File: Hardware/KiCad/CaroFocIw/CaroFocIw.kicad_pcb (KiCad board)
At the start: 4 copper layers, 174.5 x 99 mm, 110 parts, among them J1 Conn_01x04, J10 Conn_01x03, J11 Conn_01x06, J12 Conn_01x06, J13 Conn_01x02, J14 Conn_01x03, J15 Conn_01x03, J16 Conn_01x03, J17 Conn_01x02, J18 Conn_01x03, J19 Conn_01x03, J2 Conn_01x02, J20 Conn_01x03, J21 Conn_01x06, J22 Conn_01x06, J23 Conn_01x02, J24 Conn_01x03, J25 Conn_01x03, J26 Conn_01x03, J3 Conn_01x01, J4 Conn_01x01, J5 Conn_01x01, J6 Conn_01x01, J7 Conn_01x02, J8 Conn_01x03, J9 Conn_01x03, Q1 Q_NMOS_SGD, Q2 Q_NMOS_SGD, Q3 Q_NMOS_SGD, Q4 Q_NMOS_SGD, Q5 Q_NMOS_SGD, Q6 Q_NMOS_SGD, U1 TCAN332, U2 STM32F405RGTx, U3 TLE7185-1E, U4 ACS711xEXLT-15AB, U5 AS5048A, U6 ACS711xEXLT-15AB, U7 ACS711xEXLT-15AB, U8 LMR16006YQ3

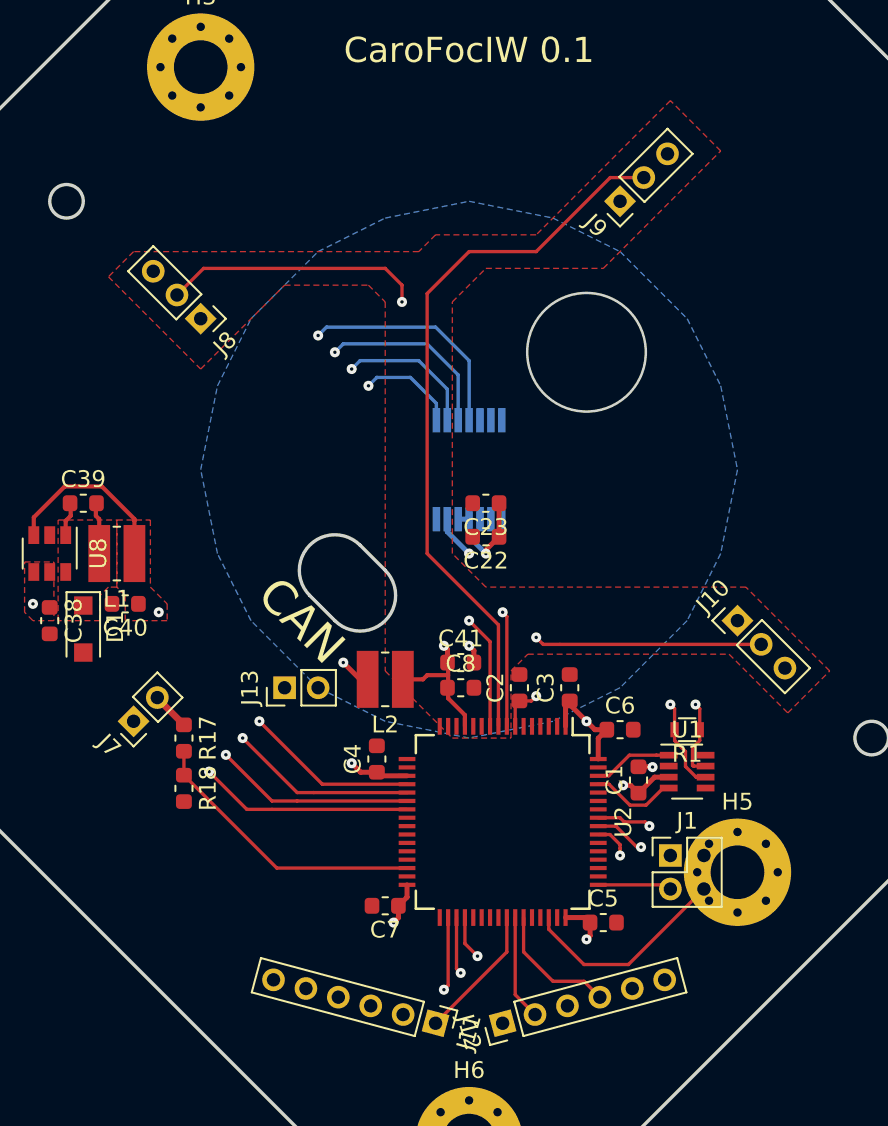
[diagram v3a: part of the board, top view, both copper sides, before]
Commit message: Changed footprint of one inductor, rerouted microcontroller part. Mounting hole placement still needs some thoughts...
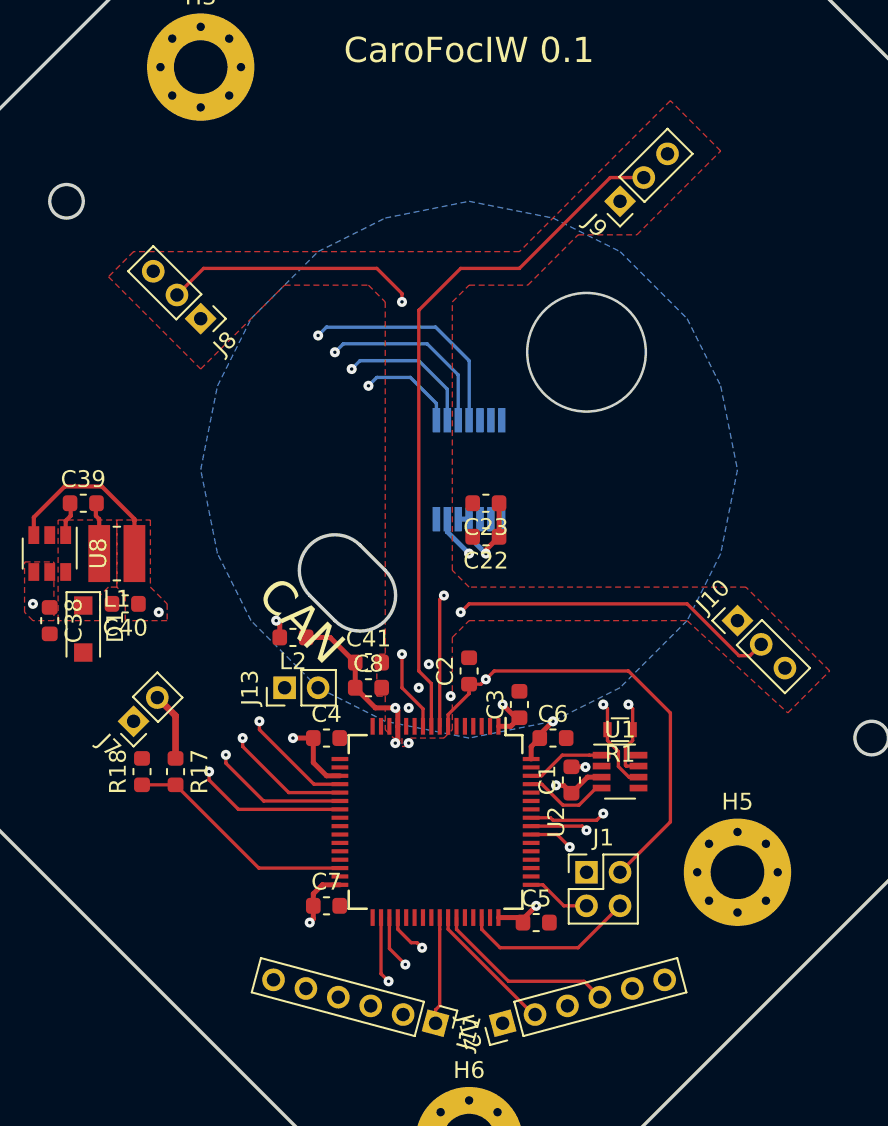
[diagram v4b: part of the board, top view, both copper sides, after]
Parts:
- L2: footprint Inductors_SMD:L_Wuerth_MAPI-3015 -> Inductor_SMD:L_0603_1608Metric
- moved L2 6.04 mm to (109.5, 135.0)
- moved C41 5.50 mm to (114.0, 136.5)
- moved C8 5.50 mm to (114.0, 138.0)
- moved J1 5.10 mm to (127.0, 149.0)
- moved C6 4.03 mm to (125.0, 141.0)
- moved C1 4.00 mm to (126.1, 143.5)
- moved C5 4.00 mm to (124.0, 152.0)
- moved R1 4.00 mm to (129.0, 140.5)
- moved U1 4.00 mm to (129.0, 143.0)
- moved U2 4.00 mm to (118.0, 146.0)
- moved C7 3.50 mm to (111.5, 151.0), turned to 0 degrees
- moved C4 3.25 mm to (111.5, 141.0), turned to 0 degrees
- moved C2 3.16 mm to (120.0, 137.0)
- moved C3 3.16 mm to (123.0, 139.0)
- moved R18 2.69 mm to (100.5, 143.0), turned to 90 degrees
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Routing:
- net /MCU/CurrentW: track 24.8 -> 29.0 mm
- net /Encoder/EncoderMiso: track 50.1 -> 46.4 mm
- net /Encoder/~EncoderCs: track 39.4 -> 35.7 mm
- net /Encoder/EncoderMosi: track 55.4 -> 51.7 mm
- net /Encoder/EncoderSclk: track 44.7 -> 41.0 mm
- net /Can/CanL: track 29.4 -> 25.8 mm
- net /MCU/LogicWL: track 12.6 -> 16.1 mm
- net /MCU/LogicVL: track 10.6 -> 13.9 mm
- net /Can/CanH: track 33.4 -> 30.1 mm
- net /MCU/LogicWH: track 7.71 -> 10.9 mm
- net /DcLinkVoltageSensing/AnalogOut: track 17.0 -> 13.9 mm
- net /MCU/LogicUL: track 8.73 -> 11.8 mm
- net /MCU/SWDIO: track 12.7 -> 10.4 mm
- net +3.3VA: track 8.11 -> 10.2 mm, vias 1 -> 2
- net /MCU/CurrentU: track 43.7 -> 41.6 mm
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
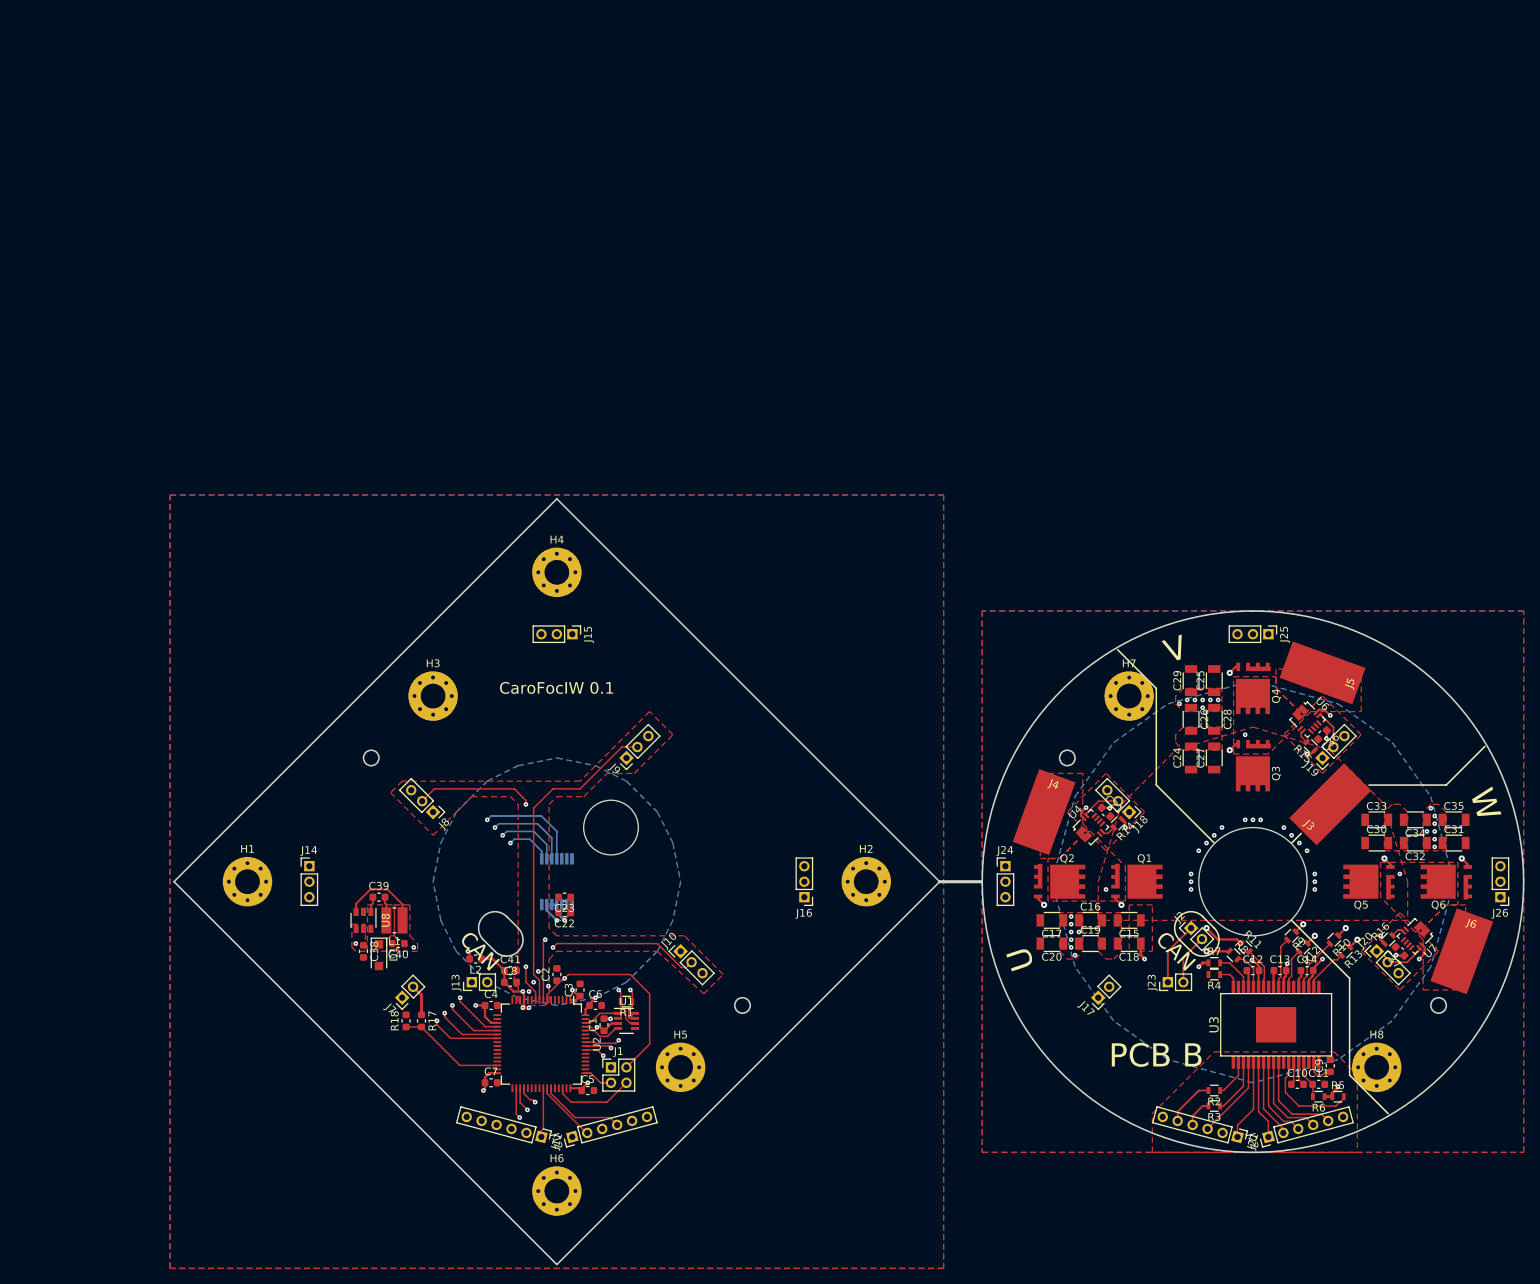
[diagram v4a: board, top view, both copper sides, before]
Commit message: More capacitors, no airwires left (old form factor)
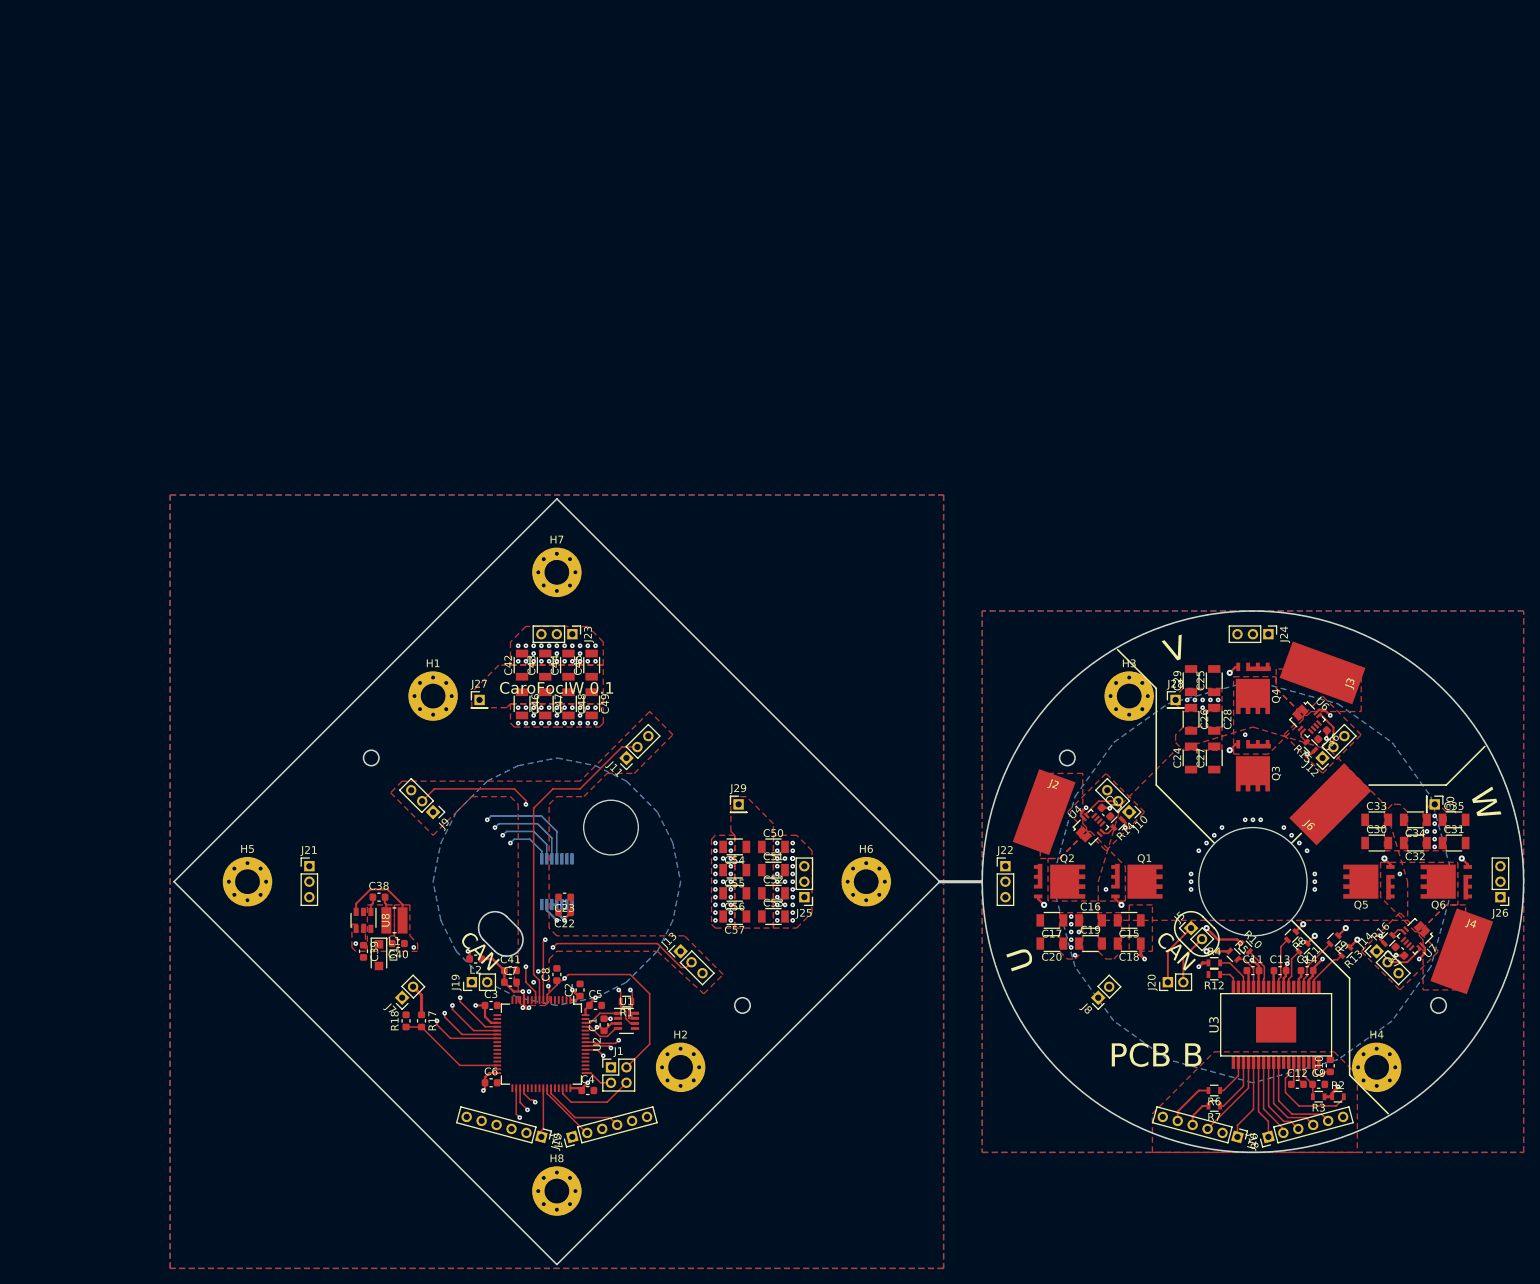
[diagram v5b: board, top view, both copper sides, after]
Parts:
- added C42: 22μ, 25V, Capacitors_SMD:C_1206, F.Cu at (115.5, 97.0)
- added C43: 22μ, 25V, Capacitors_SMD:C_1206, F.Cu at (118.5, 97.0)
- added C44: 22μ, 25V, Capacitors_SMD:C_1206, F.Cu at (121.5, 97.0)
- added C45: 22μ, 25V, Capacitors_SMD:C_1206, F.Cu at (124.5, 97.0)
- added C46: 22μ, 25V, Capacitors_SMD:C_1206, F.Cu at (115.5, 102.0)
- added C47: 22μ, 25V, Capacitors_SMD:C_1206, F.Cu at (118.5, 102.0)
- added C48: 22μ, 25V, Capacitors_SMD:C_1206, F.Cu at (121.5, 102.0)
- added C49: 22μ, 25V, Capacitors_SMD:C_1206, F.Cu at (124.5, 102.0)
- added C50: 22μ, 25V, Capacitors_SMD:C_1206, F.Cu at (148.0, 120.5)
- added C51: 22μ, 25V, Capacitors_SMD:C_1206, F.Cu at (148.0, 123.5)
- added C52: 22μ, 25V, Capacitors_SMD:C_1206, F.Cu at (148.0, 126.5)
- added C53: 22μ, 25V, Capacitors_SMD:C_1206, F.Cu at (148.0, 129.5)
- added C54: 22μ, 25V, Capacitors_SMD:C_1206, F.Cu at (143.0, 120.5)
- added C55: 22μ, 25V, Capacitors_SMD:C_1206, F.Cu at (143.0, 123.5)
- added C56: 22μ, 25V, Capacitors_SMD:C_1206, F.Cu at (143.0, 126.5)
- added C57: 22μ, 25V, Capacitors_SMD:C_1206, F.Cu at (143.0, 129.5)
- added J27: Conn_01x01, Connector_PinHeader_2.00mm:PinHeader_1x01_P2.00mm_Vertical, F.Cu at (110.0, 101.5)
- added J28: Conn_01x01, Connector_PinHeader_2.00mm:PinHeader_1x01_P2.00mm_Vertical, F.Cu at (200.0, 101.5)
- added J29: Conn_01x01, Connector_PinHeader_2.00mm:PinHeader_1x01_P2.00mm_Vertical, F.Cu at (143.5, 115.0)
- added J30: Conn_01x01, Connector_PinHeader_2.00mm:PinHeader_1x01_P2.00mm_Vertical, F.Cu at (233.5, 115.0)
- renumbered C9 to C10, C12 to C11, C10 to C12, C3 to C2, C4 to C3, C39 to C38, C38 to C39, C5 to C4, C6 to C5, C7 to C6, C8 to C7, C2 to C8, C11 to C9, H3 to H1, H5 to H2, H7 to H3, H8 to H4, H1 to H5, H2 to H6, H4 to H7, H6 to H8, J18 to J10, J9 to J11, J19 to J12, J10 to J13, J20 to J14, J11 to J15, J21 to J16, J12 to J17, J22 to J18, J13 to J19, J4 to J2, J23 to J20, J14 to J21, J24 to J22, J15 to J23, J25 to J24, J16 to J25, J5 to J3, J6 to J4, J2 to J5, J3 to J6, J17 to J8, J8 to J9, R11 to R10, R12 to R11, R4 to R12, R5 to R2, R6 to R3, R7 to R4, R8 to R5, R2 to R6, R3 to R7, R9 to R8, R10 to R9
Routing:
- net GNDPWR_A: vias 0 -> 102
- net +BATT: vias 41 -> 39
- added copper zone on F.Cu, net BattA1
- added copper zone on F.Cu, net BattA2
- added copper zone on F.Cu, net GNDPWR_A
